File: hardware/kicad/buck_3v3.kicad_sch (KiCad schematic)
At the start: 8 parts, among them U1 PTSM82903SISB2R

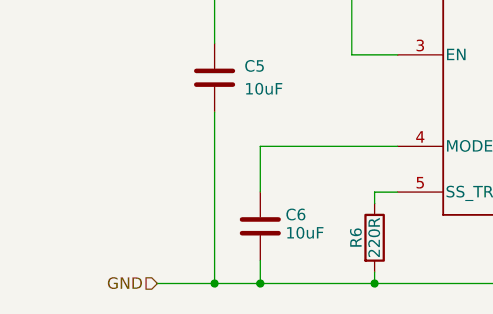
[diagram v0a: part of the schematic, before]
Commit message: feat: added buck converter 12V to 5V
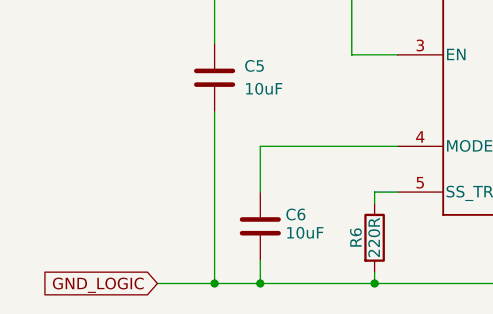
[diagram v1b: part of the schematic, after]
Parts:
- U1: footprint Regulators:SIS0011A-MFG -> Buck-3V3:SIS0011A-MFG
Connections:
- net GND renamed GND_LOGIC
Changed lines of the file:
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@@
+	(wire
+		(pts
+			(xy 184.15 72.39) (xy 184.15 80.01)
+		)
+		(stroke
+			(width 0)
+			(type default)
+		)
+	)
+	(wire
+		(pts
+			(xy 156.21 74.93) (xy 160.02 74.93)
+		)
+		(stroke
+			(width 0)
+			(type default)
+		)
+	)
+	(wire
+		(pts
+			(xy 173.99 107.95) (xy 173.99 97.79)
+		)
+		(stroke
+			(width 0)
+			(type default)
+		)
+	)
+	(wire
+		(pts
+			(xy 157.48 92.71) (xy 156.21 92.71)
+		)
+		(stroke
+			(width 0)
+			(type default)
+		)
+	)
+	(wire
+		(pts
+			(xy 118.11 107.95) (xy 173.99 107.95)
+		)
+		(stroke
+			(width 0)
+			(type default)
+		)
+	)
+	(wire
+		(pts
+			(xy 120.65 74.93) (xy 115.57 74.93)
+		)
+		(stroke
+			(width 0)
+			(type default)
+		)
+	)
+	(wire
+		(pts
+			(xy 120.65 97.79) (xy 118.11 97.79)
+		)
+		(stroke
+			(width 0)
+			(type default)
+		)
+	)
+	(wire
+		(pts
+			(xy 165.1 92.71) (xy 166.37 92.71)
+		)
+		(stroke
+			(width 0)
+			(type default)
+		)
+	)
+	(wire
+		(pts
+			(xy 173.99 97.79) (xy 173.99 91.44)
+		)
+		(stroke
+			(width 0)
+			(type default)
+		)
+	)
+	(wire
+		(pts
+			(xy 105.41 107.95) (xy 118.11 107.95)
+		)
+		(stroke
+			(width 0)
+			(type default)
+		)
+	)
+	(wire
+		(pts
+			(xy 120.65 82.55) (xy 115.57 82.55)
+		)
+		(stroke
+			(width 0)
+			(type default)
+		)
+	)
+	(wire
+		(pts
+			(xy 95.25 72.39) (xy 100.33 72.39)
+		)
+		(stroke
+			(width 0)
+			(type default)
+		)
+	)
+	(wire
+		(pts
+			(xy 184.15 87.63) (xy 184.15 97.79)
+		)
+		(stroke
+			(width 0)
+			(type default)
+		)
+	)
+	(wire
+		(pts
+			(xy 118.11 97.79) (xy 118.11 99.06)
+		)
+		(stroke
+			(width 0)
+			(type default)
+		)
+	)
 	(wire
 		(pts
@@
 	(wire
 		(pts
-			(xy 184.15 72.39) (xy 184.15 80.01)
-		)
-		(stroke
-			(width 0)
-			(type default)
-		)
-	)
-	(wire
-		(pts
-			(xy 156.21 74.93) (xy 160.02 74.93)
-		)
-		(stroke
-			(width 0)
-			(type default)
-		)
-	)
-	(wire
-		(pts
-			(xy 173.99 107.95) (xy 173.99 97.79)
-		)
-		(stroke
-			(width 0)
-			(type default)
-		)
-	)
-	(wire
-		(pts
-			(xy 157.48 92.71) (xy 156.21 92.71)
-		)
-		(stroke
-			(width 0)
-			(type default)
-		)
-	)
-	(wire
-		(pts
-			(xy 118.11 107.95) (xy 173.99 107.95)
-		)
-		(stroke
-			(width 0)
-			(type default)
-		)
-	)
-	(wire
-		(pts
-			(xy 120.65 74.93) (xy 115.57 74.93)
-		)
-		(stroke
-			(width 0)
-			(type default)
-		)
-	)
-	(wire
-		(pts
-			(xy 120.65 97.79) (xy 118.11 97.79)
-		)
-		(stroke
-			(width 0)
-			(type default)
-		)
-	)
-	(wire
-		(pts
-			(xy 165.1 92.71) (xy 166.37 92.71)
-		)
-		(stroke
-			(width 0)
-			(type default)
-		)
-	)
-	(wire
-		(pts
-			(xy 173.99 97.79) (xy 173.99 91.44)
-		)
-		(stroke
-			(width 0)
-			(type default)
-		)
-	)
-	(wire
-		(pts
-			(xy 105.41 107.95) (xy 118.11 107.95)
-		)
-		(stroke
-			(width 0)
-			(type default)
-		)
-	)
-	(wire
-		(pts
-			(xy 120.65 82.55) (xy 115.57 82.55)
-		)
-		(stroke
-			(width 0)
-			(type default)
-		)
-	)
-	(wire
-		(pts
-			(xy 95.25 72.39) (xy 100.33 72.39)
-		)
-		(stroke
-			(width 0)
-			(type default)
-		)
-	)
-	(wire
-		(pts
-			(xy 184.15 87.63) (xy 184.15 97.79)
-		)
-		(stroke
-			(width 0)
-			(type default)
-		)
-	)
-	(wire
-		(pts
-			(xy 118.11 97.79) (xy 118.11 99.06)
-		)
-		(stroke
-			(width 0)
-			(type default)
-		)
-	)
-	(wire
-		(pts
 			(xy 100.33 72.39) (xy 100.33 81.28)
 		)
@@
 			(width 0)
 			(type default)
+		)
+	)
+	(global_label "GND_LOGIC"
+		(shape input)
+		(at 93.98 107.95 180)
+		(fields_autoplaced yes)
+		(effects
+			(font
+				(size 1.27 1.27)
+			)
+			(justify right)
+		)
+		(property "Intersheetrefs" "${INTERSHEET_REFS}"
+			(at 80.6533 107.95 0)
+			(effects
+				(font
+					(size 1.27 1.27)
+				)
+				(justify right)
+				(hide yes)
+			)
 		)
 	)
@@
 			)
 			(justify left)
-		)
-	)
-	(hierarchical_label "GND"
-		(shape input)
-		(at 93.98 107.95 180)
-		(effects
-			(font
-				(size 1.27 1.27)
-			)
-			(justify right)
 		)
 	)
@@
 			)
 		)
-		(property "Footprint" "Regulators:SIS0011A-MFG"
+		(property "Footprint" "Buck-3V3:SIS0011A-MFG"
 			(at 120.65 72.39 0)
 			(effects

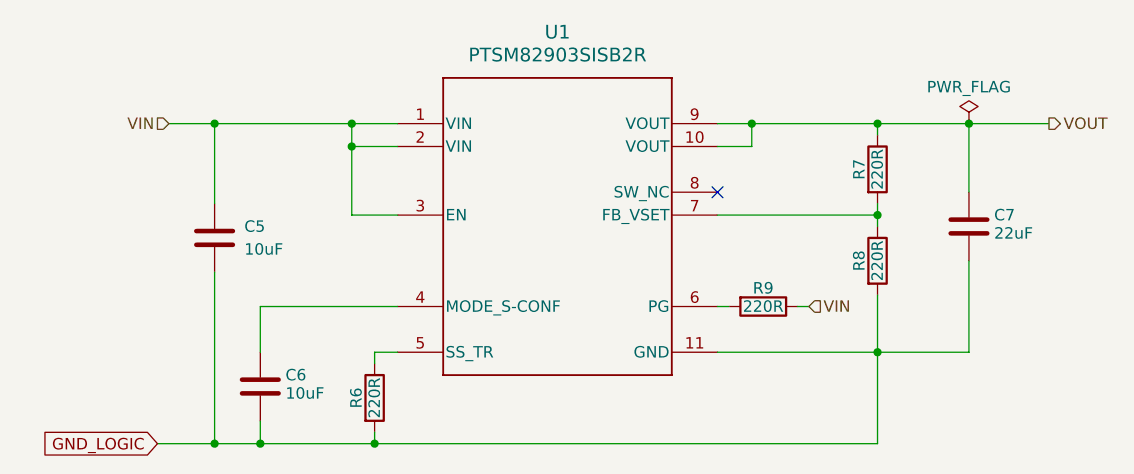
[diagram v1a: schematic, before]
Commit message: fix: footprint issues and library conflicts - KiCAD
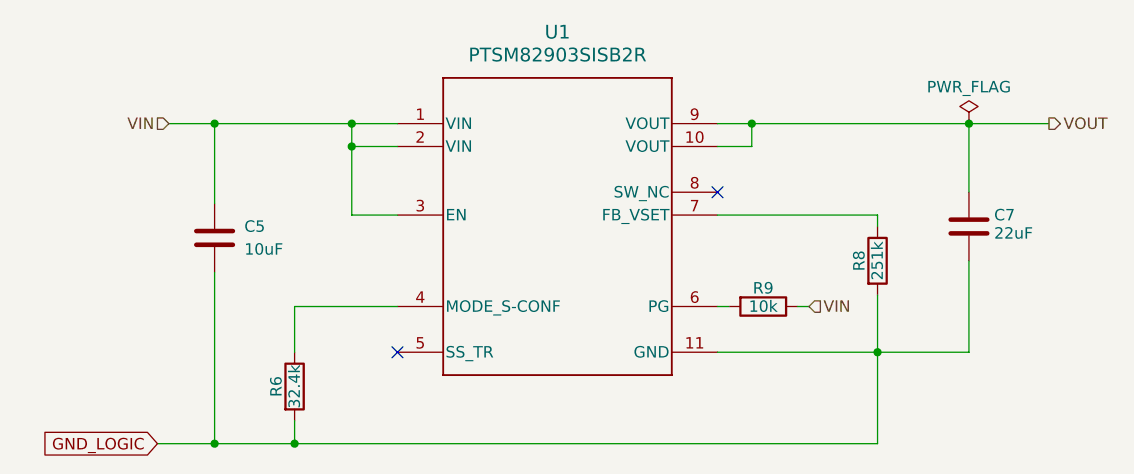
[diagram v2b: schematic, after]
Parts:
- removed C6: 10uF, Capacitor_THT:C_Rect_L4.0mm_W2.5mm_P2.50mm, symbol Device:C
- removed R7: 220R, symbol Device:R
- R6: value 220R -> 32.4k
- R8: value 220R -> 251k
- R9: value 220R -> 10k
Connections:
- net at R6.1: now also U1.4 (MODE_S-CONF); no longer U1.5 (SS_TR)
- no-connect marks 1 -> 2
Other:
- moved on the sheet: R6

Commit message: feat: separated modules but added power module
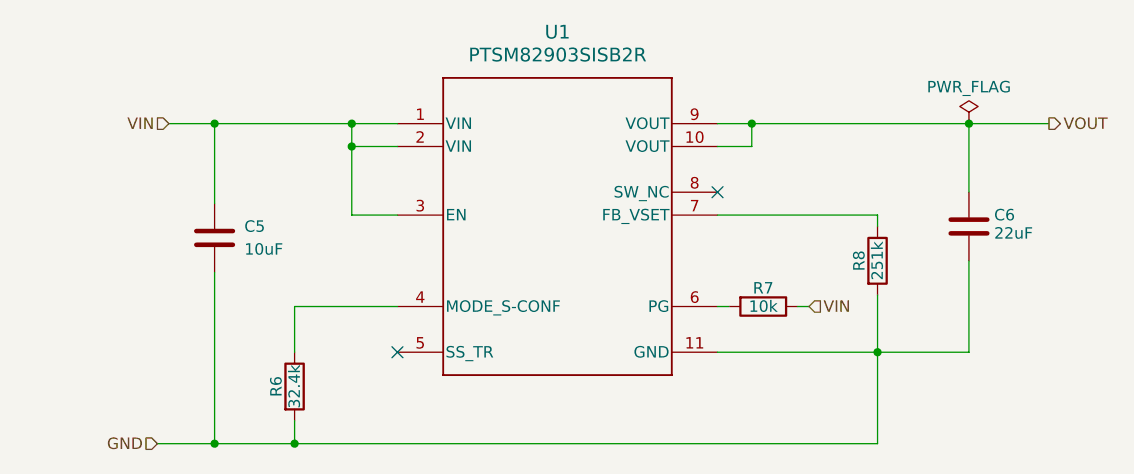
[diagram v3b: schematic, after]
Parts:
- R6, R8: footprint (none) -> Resistor_THT:R_Axial_DIN0207_L6.3mm_D2.5mm_P2.54mm_Vertical
- R7: renamed from R9; footprint (none) -> Resistor_THT:R_Axial_DIN0207_L6.3mm_D2.5mm_P2.54mm_Vertical
- renumbered C7 to C6
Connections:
- net GND_LOGIC renamed GND
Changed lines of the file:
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@@
 		)
 	)
-	(global_label "GND_LOGIC"
+	(hierarchical_label "GND"
 		(shape input)
 		(at 93.98 107.95 180)
-		(fields_autoplaced yes)
 		(effects
 			(font
@@
 			)
 			(justify right)
-		)
-		(property "Intersheetrefs" "${INTERSHEET_REFS}"
-			(at 80.6533 107.95 0)
-			(effects
-				(font
-					(size 1.27 1.27)
-				)
-				(justify right)
-				(hide yes)
-			)
 		)
 	)
@@
 		(on_board yes)
 		(dnp no)
-		(property "Reference" "R9"
+		(property "Reference" "R7"
 			(at 161.29 90.678 90)
 			(effects
@@
 			)
 		)
-		(property "Footprint" ""
+		(property "Footprint" "Resistor_THT:R_Axial_DIN0207_L6.3mm_D2.5mm_P2.54mm_Vertical"
 			(at 161.29 90.932 90)
 			(effects
@@
 		)
 		(instances
-			(project "card_issuance"
-				(path "/efd10ce8-d30e-4563-b475-2afafc95cd2b/d6ed446d-e13a-4330-af37-f0669133989b/c173e131-e50a-4512-9a94-e35264276009"
-					(reference "R9")
+			(project "card_issuance_power"
+				(path "/eccaacbb-6cc6-4795-9ce3-6b61aaecb3e3/ff3970ec-c005-431d-9ba7-afce8ead4fbb"
+					(reference "R7")
 					(unit 1)
 				)
@@
 		)
 		(instances
-			(project "card_issuance"
-				(path "/efd10ce8-d30e-4563-b475-2afafc95cd2b/d6ed446d-e13a-4330-af37-f0669133989b/c173e131-e50a-4512-9a94-e35264276009"
+			(project "card_issuance_power"
+				(path "/eccaacbb-6cc6-4795-9ce3-6b61aaecb3e3/ff3970ec-c005-431d-9ba7-afce8ead4fbb"
 					(reference "C5")
 					(unit 1)
@@
 			)
 		)
-		(property "Footprint" ""
+		(property "Footprint" "Resistor_THT:R_Axial_DIN0207_L6.3mm_D2.5mm_P2.54mm_Vertical"
 			(at 107.442 101.6 90)
 			(effects
@@
 		)
 		(instances
-			(project "card_issuance"
-				(path "/efd10ce8-d30e-4563-b475-2afafc95cd2b/d6ed446d-e13a-4330-af37-f0669133989b/c173e131-e50a-4512-9a94-e35264276009"
+			(project "card_issuance_power"
+				(path "/eccaacbb-6cc6-4795-9ce3-6b61aaecb3e3/ff3970ec-c005-431d-9ba7-afce8ead4fbb"
 					(reference "R6")
 					(unit 1)
@@
 		)
 		(instances
-			(project ""
-				(path "/efd10ce8-d30e-4563-b475-2afafc95cd2b/d6ed446d-e13a-4330-af37-f0669133989b/c173e131-e50a-4512-9a94-e35264276009"
+			(project "card_issuance_power"
+				(path "/eccaacbb-6cc6-4795-9ce3-6b61aaecb3e3/ff3970ec-c005-431d-9ba7-afce8ead4fbb"
 					(reference "U1")
 					(unit 1)
@@
 		(on_board yes)
 		(dnp no)
-		(property "Reference" "C7"
+		(property "Reference" "C6"
 			(at 186.944 82.55 0)
 			(effects
@@
 		)
 		(instances
-			(project "card_issuance"
-				(path "/efd10ce8-d30e-4563-b475-2afafc95cd2b/d6ed446d-e13a-4330-af37-f0669133989b/c173e131-e50a-4512-9a94-e35264276009"
-					(reference "C7")
+			(project "card_issuance_power"
+				(path "/eccaacbb-6cc6-4795-9ce3-6b61aaecb3e3/ff3970ec-c005-431d-9ba7-afce8ead4fbb"
+					(reference "C6")
 					(unit 1)
 				)
@@
 		)
 		(instances
-			(project ""
-				(path "/efd10ce8-d30e-4563-b475-2afafc95cd2b/d6ed446d-e13a-4330-af37-f0669133989b/c173e131-e50a-4512-9a94-e35264276009"
+			(project "card_issuance_power"
+				(path "/eccaacbb-6cc6-4795-9ce3-6b61aaecb3e3/ff3970ec-c005-431d-9ba7-afce8ead4fbb"
 					(reference "#FLG02")
 					(unit 1)
@@
 			)
 		)
-		(property "Footprint" ""
+		(property "Footprint" "Resistor_THT:R_Axial_DIN0207_L6.3mm_D2.5mm_P2.54mm_Vertical"
 			(at 172.212 87.63 90)
 			(effects
@@
 		)
 		(instances
-			(project "card_issuance"
-				(path "/efd10ce8-d30e-4563-b475-2afafc95cd2b/d6ed446d-e13a-4330-af37-f0669133989b/c173e131-e50a-4512-9a94-e35264276009"
+			(project "card_issuance_power"
+				(path "/eccaacbb-6cc6-4795-9ce3-6b61aaecb3e3/ff3970ec-c005-431d-9ba7-afce8ead4fbb"
 					(reference "R8")
 					(unit 1)

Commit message: fix: buck connections
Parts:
- U1: footprint Buck-3V3:SIS0011A-MFG -> Buck 3V3:SIS0011A-MFG
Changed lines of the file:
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@@
 			)
 		)
-		(property "Footprint" "Buck-3V3:SIS0011A-MFG"
+		(property "Footprint" "Buck 3V3:SIS0011A-MFG"
 			(at 120.65 72.39 0)
 			(effects
